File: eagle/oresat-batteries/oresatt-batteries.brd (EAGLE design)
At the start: 94 x 93.5 mm, 8 parts, among them U1 TCAN330

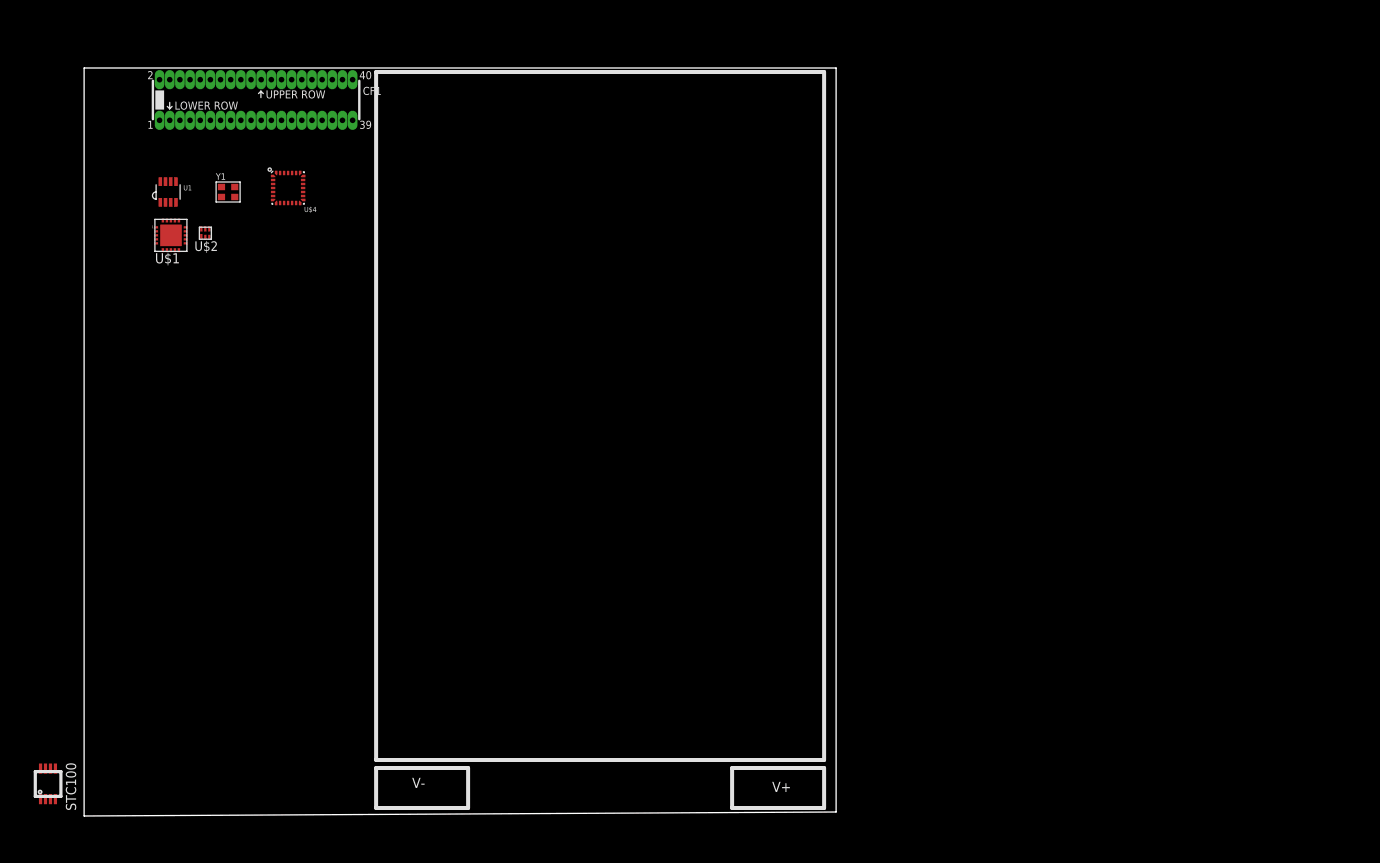
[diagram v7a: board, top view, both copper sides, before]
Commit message: Started rough layout of boards. Updated design docs (see google docs)
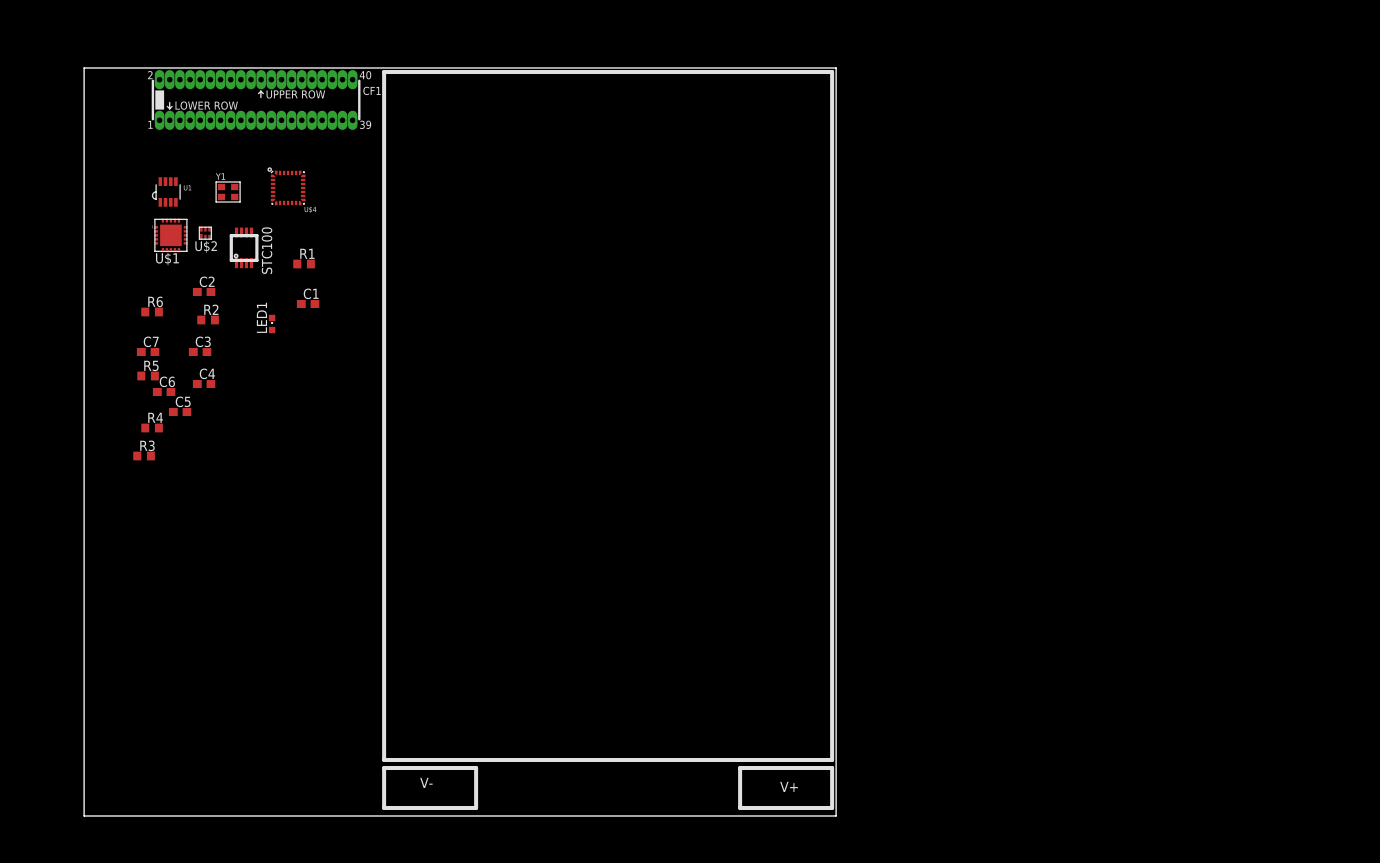
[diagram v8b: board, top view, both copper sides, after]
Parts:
- added C1, C2, C3, C4, C5, C6, C7: (no value), rcl:C0603
- added LED1: (no value), led:CHIPLED_0603
- added R1, R3, R4: Sense, rcl:R0603
- added R2, R5, R6: (no value), rcl:R0603
- moved U$5 71.3 mm to (20.0, 71.0)
- moved U$3 1.00 mm to (65.5, 50.0)
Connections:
- new net N$1: R1.2, U$1.18
- new net N$10: R6.1, U$2.6
- new net N$2: LED1.A, R2.2
- new net N$3: LED1.C, U$1.15
- new net N$4: C3.1, CF1.P$1, U$1.10, U$1.11, U$1.9
- new net N$5: C5.1, CF1.P$3, U$1.6, U$1.7, U$1.8
- new net N$6: C4.1
- new net N$7: R4.2, U$5.2
- new net N$8: R3.2
- new net N$9: C6.2, R5.2, U$5.8
- new net VBAT+: C1.1, C2.1, C7.2, R5.1, U$1.12, U$1.13, U$1.14, U$1.4, U$2.5, U$5.7
- net GND: now also C1.2, C2.2, C3.2, C4.2, C5.2, C6.1, C7.1, R1.1, R2.1, R3.1, R4.1, R6.2, U$1.20, U$1.P$1, U$2.4, U$5.5
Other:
- outline, holes or cut-outs redrawn
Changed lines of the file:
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@@
 <board>
 <plain>
-<wire x1="0" y1="0" x2="94" y2="0.5" width="0" layer="20"/>
-<wire x1="94" y1="0.5" x2="94" y2="93.5" width="0" layer="20"/>
+<wire x1="0" y1="0" x2="94" y2="0" width="0" layer="20"/>
+<wire x1="94" y1="0" x2="94" y2="93.5" width="0" layer="20"/>
 <wire x1="94" y1="93.5" x2="0" y2="93.5" width="0" layer="20"/>
 <wire x1="0" y1="93.5" x2="0" y2="0" width="0" layer="20"/>
@@
 <element name="Y1" library="low-gain-radio" package="CRYSTAL_2.5X2" value="" x="18" y="78"/>
 <element name="CF1" library="low-gain-radio" package="HARWIN-ARCHER-M50-3202045" value="ORESAT-CONNECTOR-40PIN" x="21.5" y="89.5"/>
-<element name="U$5" library="oresat-batteries" package="MINISO-8" value="STC3100LST" x="-4.5" y="4"/>
-<element name="U$3" library="oresat-batteries" package="1.5AH" value="1.5AHBATT" x="64.5" y="50"/>
+<element name="U$5" library="oresat-batteries" package="MINISO-8" value="STC3100LST" x="20" y="71"/>
+<element name="U$3" library="oresat-batteries" package="1.5AH" value="1.5AHBATT" x="65.5" y="50"/>
+<element name="R1" library="rcl" package="R0603" value="Sense" x="27.5" y="69"/>
+<element name="C1" library="rcl" package="C0603" value="" x="28" y="64"/>
+<element name="C2" library="rcl" package="C0603" value="" x="15" y="65.5"/>
+<element name="LED1" library="led" package="CHIPLED_0603" value="" x="23.5" y="61.5"/>
+<element name="R2" library="rcl" package="R0603" value="" x="15.5" y="62"/>
+<element name="C3" library="rcl" package="C0603" value="" x="14.5" y="58"/>
+<element name="C4" library="rcl" package="C0603" value="" x="15" y="54"/>
+<element name="C5" library="rcl" package="C0603" value="" x="12" y="50.5"/>
+<element name="R3" library="rcl" package="R0603" value="Sense" x="7.5" y="45"/>
+<element name="R4" library="rcl" package="R0603" value="Sense" x="8.5" y="48.5"/>
+<element name="C6" library="rcl" package="C0603" value="" x="10" y="53"/>
+<element name="R5" library="rcl" package="R0603" value="" x="8" y="55"/>
+<element name="C7" library="rcl" package="C0603" value="" x="8" y="58"/>
+<element name="R6" library="rcl" package="R0603" value="" x="8.5" y="63"/>
 </elements>
 <signals>
@@
 <signal name="GND">
 <contactref element="U1" pad="2"/>
+<contactref element="U$1" pad="P$1"/>
+<contactref element="U$1" pad="20"/>
+<contactref element="R1" pad="1"/>
+<contactref element="C2" pad="2"/>
+<contactref element="R2" pad="1"/>
+<contactref element="C3" pad="2"/>
+<contactref element="C4" pad="2"/>
+<contactref element="C5" pad="2"/>
+<contactref element="R3" pad="1"/>
+<contactref element="R4" pad="1"/>
+<contactref element="U$5" pad="5"/>
+<contactref element="C6" pad="1"/>
+<contactref element="C7" pad="1"/>
+<contactref element="R6" pad="2"/>
+<contactref element="U$2" pad="4"/>
+<contactref element="C1" pad="2"/>
+<wire x1="15.66" y1="73.375" x2="20.915" y2="72.92" width="0" layer="19" extent="1-1"/>
+<wire x1="10.85" y1="72.58" x2="15.66" y2="73.375" width="0" layer="19" extent="1-1"/>
+<wire x1="9.85" y1="74.43" x2="10.85" y2="72.58" width="0" layer="19" extent="1-1"/>
+<wire x1="10.175" y1="76.7" x2="9.85" y2="74.43" width="0" layer="19" extent="1-1"/>
+<wire x1="26.65" y1="69" x2="10.85" y2="72.58" width="0" layer="19" extent="1-1"/>
+<wire x1="28.85" y1="64" x2="26.65" y2="69" width="0" layer="19" extent="1-1"/>
+<wire x1="15.85" y1="65.5" x2="28.85" y2="64" width="0" layer="19" extent="1-1"/>
+<wire x1="14.65" y1="62" x2="15.85" y2="65.5" width="0" layer="19" extent="1-1"/>
+<wire x1="15.35" y1="58" x2="14.65" y2="62" width="0" layer="19" extent="1-1"/>
+<wire x1="15.85" y1="54" x2="15.35" y2="58" width="0" layer="19" extent="1-1"/>
+<wire x1="12.85" y1="50.5" x2="15.85" y2="54" width="0" layer="19" extent="1-1"/>
+<wire x1="6.65" y1="45" x2="12.85" y2="50.5" width="0" layer="19" extent="1-1"/>
+<wire x1="7.65" y1="48.5" x2="6.65" y2="45" width="0" layer="19" extent="1-1"/>
+<wire x1="9.15" y1="53" x2="7.65" y2="48.5" width="0" layer="19" extent="1-1"/>
+<wire x1="7.15" y1="58" x2="9.15" y2="53" width="0" layer="19" extent="1-1"/>
+<wire x1="9.35" y1="63" x2="7.15" y2="58" width="0" layer="19" extent="1-1"/>
 </signal>
 <signal name="VCC">
 <contactref element="U1" pad="3"/>
 </signal>
+<signal name="N$1">
+<contactref element="U$1" pad="18"/>
+<contactref element="R1" pad="2"/>
+<wire x1="28.35" y1="69" x2="10.85" y2="74.43" width="0" layer="19" extent="1-1"/>
+</signal>
+<signal name="VBAT+">
+<contactref element="U$1" pad="4"/>
+<contactref element="U$1" pad="12"/>
+<contactref element="U$1" pad="13"/>
+<contactref element="U$1" pad="14"/>
+<contactref element="C2" pad="1"/>
+<contactref element="R5" pad="1"/>
+<contactref element="U$5" pad="7"/>
+<contactref element="C7" pad="2"/>
+<contactref element="C1" pad="1"/>
+<contactref element="U$2" pad="5"/>
+<wire x1="15.16" y1="73.375" x2="19.675" y2="72.92" width="0" layer="19" extent="1-1"/>
+<wire x1="12.7" y1="73.08" x2="15.16" y2="73.375" width="0" layer="19" extent="1-1"/>
+<wire x1="12.7" y1="72.58" x2="12.7" y2="73.08" width="0" layer="19" extent="1-1"/>
+<wire x1="12.7" y1="72.08" x2="12.7" y2="72.58" width="0" layer="19" extent="1-1"/>
+<wire x1="9" y1="72.08" x2="12.7" y2="72.08" width="0" layer="19" extent="1-1"/>
+<wire x1="27.15" y1="64" x2="9" y2="72.08" width="0" layer="19" extent="1-1"/>
+<wire x1="14.15" y1="65.5" x2="27.15" y2="64" width="0" layer="19" extent="1-1"/>
+<wire x1="7.15" y1="55" x2="14.15" y2="65.5" width="0" layer="19" extent="1-1"/>
+<wire x1="8.85" y1="58" x2="7.15" y2="55" width="0" layer="19" extent="1-1"/>
+</signal>
+<signal name="N$2">
+<contactref element="R2" pad="2"/>
+<contactref element="LED1" pad="A"/>
+<wire x1="23.5" y1="60.75" x2="16.35" y2="62" width="0" layer="19" extent="1-1"/>
+</signal>
+<signal name="N$3">
+<contactref element="LED1" pad="C"/>
+<contactref element="U$1" pad="15"/>
+<wire x1="23.5" y1="62.25" x2="12.7" y2="73.58" width="0" layer="19" extent="1-1"/>
+</signal>
+<signal name="N$4">
+<contactref element="U$1" pad="10"/>
+<contactref element="U$1" pad="9"/>
+<contactref element="U$1" pad="11"/>
+<contactref element="CF1" pad="P$1"/>
+<contactref element="C3" pad="1"/>
+<wire x1="12.7" y1="71.58" x2="9.435" y2="86.96" width="0" layer="19" extent="1-1"/>
+<wire x1="11.85" y1="70.73" x2="12.7" y2="71.58" width="0" layer="19" extent="1-1"/>
+<wire x1="11.35" y1="70.73" x2="11.85" y2="70.73" width="0" layer="19" extent="1-1"/>
+<wire x1="13.65" y1="58" x2="11.35" y2="70.73" width="0" layer="19" extent="1-1"/>
+</signal>
+<signal name="N$5">
+<contactref element="CF1" pad="P$3"/>
+<contactref element="U$1" pad="8"/>
+<contactref element="U$1" pad="6"/>
+<contactref element="U$1" pad="7"/>
+<contactref element="C5" pad="1"/>
+<wire x1="10.85" y1="70.73" x2="10.705" y2="86.96" width="0" layer="19" extent="1-1"/>
+<wire x1="10.35" y1="70.73" x2="10.85" y2="70.73" width="0" layer="19" extent="1-1"/>
+<wire x1="9.85" y1="70.73" x2="10.35" y2="70.73" width="0" layer="19" extent="1-1"/>
+<wire x1="11.15" y1="50.5" x2="9.85" y2="70.73" width="0" layer="19" extent="1-1"/>
+</signal>
+<signal name="N$6">
+<contactref element="C4" pad="1"/>
+</signal>
+<signal name="N$7">
+<contactref element="U$5" pad="2"/>
+<contactref element="R4" pad="2"/>
+<wire x1="9.35" y1="48.5" x2="19.675" y2="69.11" width="0" layer="19" extent="1-1"/>
+</signal>
+<signal name="N$9">
+<contactref element="U$5" pad="8"/>
+<contactref element="R5" pad="2"/>
+<contactref element="C6" pad="2"/>
+<wire x1="10.85" y1="53" x2="19.055" y2="72.92" width="0" layer="19" extent="1-1"/>
+<wire x1="8.85" y1="55" x2="10.85" y2="53" width="0" layer="19" extent="1-1"/>
+</signal>
+<signal name="N$8">
+<contactref element="R3" pad="2"/>
+</signal>
+<signal name="N$10">
+<contactref element="U$2" pad="6"/>
+<contactref element="R6" pad="1"/>
+<wire x1="7.65" y1="63" x2="14.66" y2="73.375" width="0" layer="19" extent="1-1"/>
+</signal>
 </signals>
